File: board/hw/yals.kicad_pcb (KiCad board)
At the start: 2 copper layers, 102.9 x 16.5 mm, 46 parts, among them J1 SWD, J2 UART, J3 eng, J4 power, Q1 2N7002, U1 RP2040, U2 M24C02-FMN, U3 MCP1703Ax-330xxTT, U4 W25Q32JVSS, U5 DRV8220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

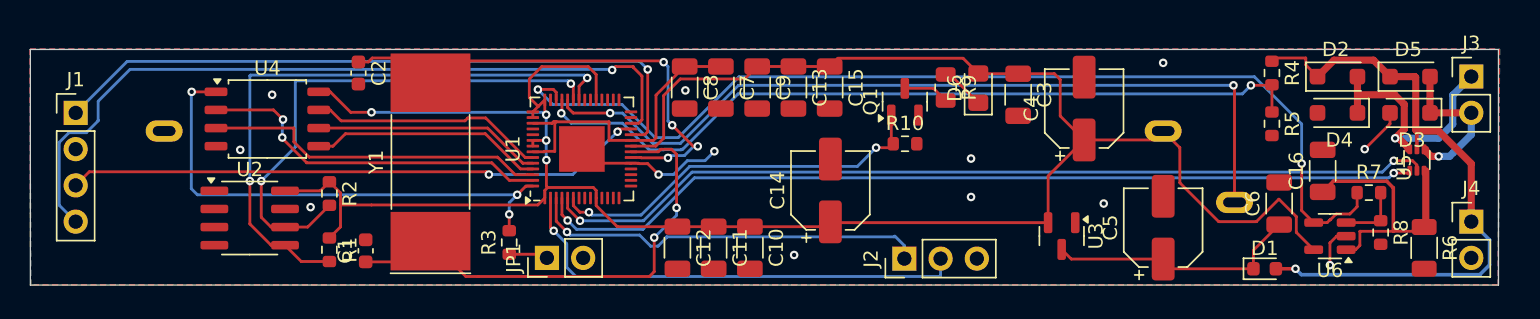
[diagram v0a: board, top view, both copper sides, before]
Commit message: increased height of the board by 1mm, to accomodate more wireing that's needed there
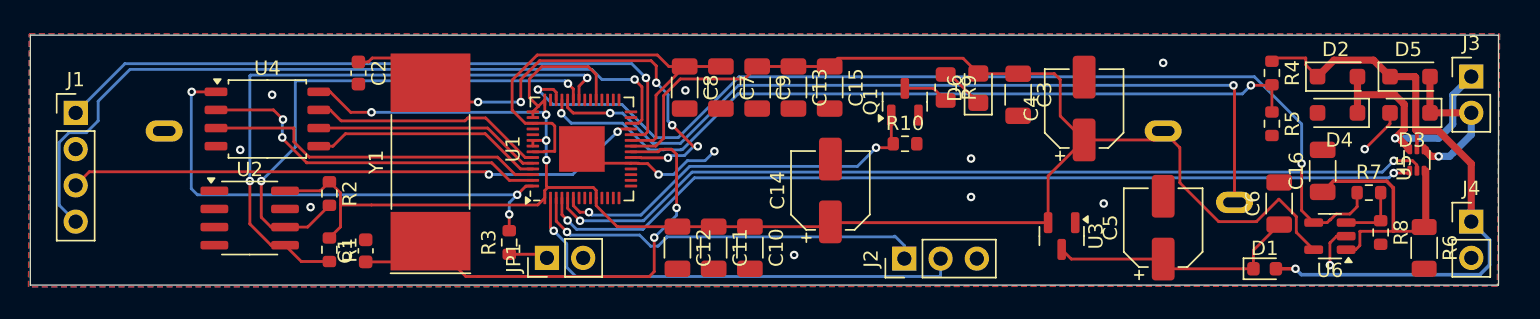
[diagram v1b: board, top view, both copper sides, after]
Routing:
- net Net-(U1-VREG_VOUT): track 22.1 -> 32.2 mm
- net Net-(U1-XIN): track 35.0 -> 38.8 mm, vias 4 -> 6
- net /microcontroller/pico_run: track 54.1 -> 53.5 mm
- net Net-(J1-Pin_1): track 47.4 -> 46.9 mm
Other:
- board size 102.9 x 16.5 mm -> 102.9 x 17.5 mm

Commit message: fixed all the DRC errors and warning on the PCB
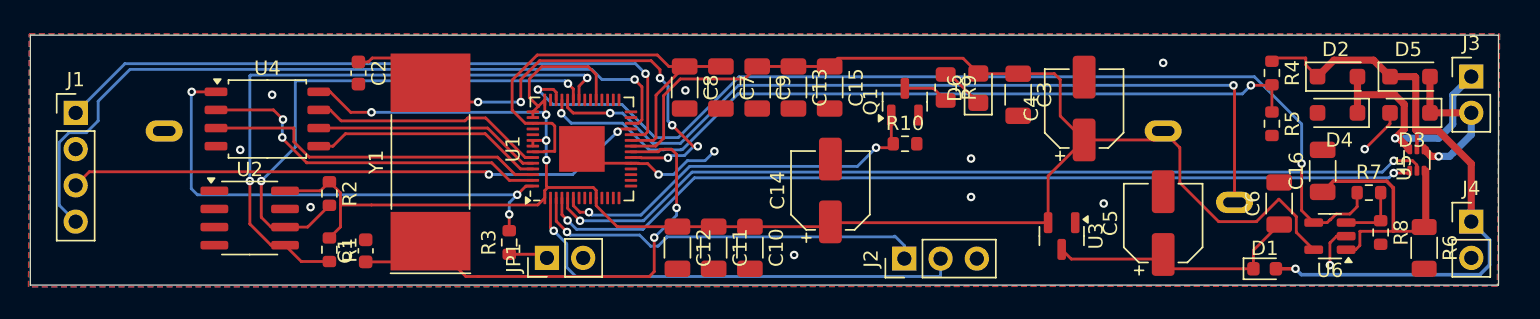
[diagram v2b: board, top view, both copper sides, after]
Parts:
- moved C5 0.32 mm to (170.2, 90.3)
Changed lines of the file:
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@@
   )
   (footprint "Capacitor_SMD:CP_Elec_5x4.5" (layer "F.Cu")
-    (at 170.18 90.592 90)
+    (at 170.18 90.2716 90)
     (descr "SMD capacitor, aluminum electrolytic, Nichicon, 5.0x4.5mm")
     (tags "capacitor electrolytic")
@@
   (segment (start 136.0836 89.7224) (end 134.5184 91.2876) (width 0.2) (layer "B.Cu") (net 36))
   (segment (start 120.375 78.905) (end 118.8425 80.4375) (width 0.2) (layer "F.Cu") (net 37))
+  (segment (start 126.485115 78.8924) (end 125.1712 80.206315) (width 0.2) (layer "F.Cu") (net 37))
+  (segment (start 134.9248 80.1116) (end 134.9248 79.520071) (width 0.2) (layer "F.Cu") (net 37))
   (segment (start 114.4812 78.981) (end 113.792 78.981) (width 0.2) (layer "F.Cu") (net 37))
   (segment (start 114.7572 78.705) (end 114.4812 78.981) (width 0.2) (layer "F.Cu") (net 37))
   (segment (start 132.8887 85.6772) (end 133.5816 85.6772) (width 0.2) (layer "F.Cu") (net 37))
-  (segment (start 126.485115 78.8924) (end 125.1712 80.206315) (width 0.2) (layer "F.Cu") (net 37))
-  (segment (start 134.297129 78.8924) (end 126.485115 78.8924) (width 0.2) (layer "F.Cu") (net 37))
-  (segment (start 134.660327 79.255598) (end 134.297129 78.8924) (width 0.2) (layer "F.Cu") (net 37))
   (segment (start 120.193 81.788) (end 118.8425 80.4375) (width 0.2) (layer "F.Cu") (net 37))
-  (segment (start 134.660327 80.440143) (end 134.660327 79.255598) (width 0.2) (layer "F.Cu") (net 37))
   (segment (start 117.11 78.705) (end 114.7572 78.705) (width 0.2) (layer "F.Cu") (net 37))
   (segment (start 118.8425 80.4375) (end 117.11 78.705) (width 0.2) (layer "F.Cu") (net 37))
@@
   (segment (start 137.255565 84.890365) (end 135.7788 83.4136) (width 0.2) (layer "F.Cu") (net 37))
   (segment (start 135.4836 85.6996) (end 133.604 85.6996) (width 0.2) (layer "F.Cu") (net 37))
+  (segment (start 137.569965 84.890365) (end 137.255565 84.890365) (width 0.2) (layer "F.Cu") (net 37))
+  (segment (start 134.9248 79.520071) (end 134.297129 78.8924) (width 0.2) (layer "F.Cu") (net 37))
+  (segment (start 122.174 81.788) (end 120.193 81.788) (width 0.2) (layer "F.Cu") (net 37))
+  (segment (start 134.297129 78.8924) (end 126.485115 78.8924) (width 0.2) (layer "F.Cu") (net 37))
   (segment (start 125.1712 80.206315) (end 125.1712 81.788) (width 0.2) (layer "F.Cu") (net 37))
-  (segment (start 137.569965 84.890365) (end 137.255565 84.890365) (width 0.2) (layer "F.Cu") (net 37))
-  (segment (start 122.174 81.788) (end 120.193 81.788) (width 0.2) (layer "F.Cu") (net 37))
   (segment (start 133.604 85.6996) (end 133.5816 85.6772) (width 0.2) (layer "F.Cu") (net 37))
   (via (at 135.4836 85.6996) (size 0.6) (drill 0.3) (layers "F.Cu" "B.Cu") (net 37))
-  (via (at 134.660327 80.440143) (size 0.6) (drill 0.3) (layers "F.Cu" "B.Cu") (net 37))
+  (via (at 134.9248 80.1116) (size 0.6) (drill 0.3) (layers "F.Cu" "B.Cu") (net 37))
   (via (at 135.7788 83.4136) (size 0.6) (drill 0.3) (layers "F.Cu" "B.Cu") (net 37))
   (via (at 122.174 81.788) (size 0.6) (drill 0.3) (layers "F.Cu" "B.Cu") (net 37))
   (via (at 125.1712 81.788) (size 0.6) (drill 0.3) (layers "F.Cu" "B.Cu") (net 37))
   (via (at 137.569965 84.890365) (size 0.6) (drill 0.3) (layers "F.Cu" "B.Cu") (net 37))
-  (segment (start 134.660327 80.440143) (end 135.4836 81.263416) (width 0.2) (layer "B.Cu") (net 37))
-  (segment (start 135.4836 83.1184) (end 135.7788 83.4136) (width 0.2) (layer "B.Cu") (net 37))
   (segment (start 137.287121 84.890365) (end 136.636685 85.5408) (width 0.2) (layer "B.Cu") (net 37))
   (segment (start 136.636685 85.5408) (end 135.6424 85.5408) (width 0.2) (layer "B.Cu") (net 37))
   (segment (start 137.569965 84.890365) (end 137.287121 84.890365) (width 0.2) (layer "B.Cu") (net 37))
   (segment (start 125.1712 81.788) (end 122.174 81.788) (width 0.2) (layer "B.Cu") (net 37))
-  (segment (start 135.4836 81.263416) (end 135.4836 83.1184) (width 0.2) (layer "B.Cu") (net 37))
+  (segment (start 135.4836 80.6704) (end 135.4836 83.1184) (width 0.2) (layer "B.Cu") (net 37))
+  (segment (start 135.4836 83.1184) (end 135.7788 83.4136) (width 0.2) (layer "B.Cu") (net 37))
+  (segment (start 134.9248 80.1116) (end 135.4836 80.6704) (width 0.2) (layer "B.Cu") (net 37))
   (segment (start 135.6424 85.5408) (end 135.4836 85.6996) (width 0.2) (layer "B.Cu") (net 37))
   (segment (start 144.272 79.297) (end 146.812 79.297) (width 0.2) (layer "F.Cu") (net 38))
@@
   (segment (start 170.86 93.472) (end 170.18 92.792) (width 0.2) (layer "F.Cu") (net 39))
   (segment (start 170.18 92.792) (end 163.744 92.792) (width 0.2) (layer "F.Cu") (net 39))
+  (segment (start 133.9088 79.8068) (end 134.0612 79.9592) (width 0.2) (layer "F.Cu") (net 40))
+  (segment (start 134.0612 83.8708) (end 133.8548 84.0772) (width 0.2) (layer "F.Cu") (net 40))
   (segment (start 133.8548 84.0772) (end 132.8887 84.0772) (width 0.2) (layer "F.Cu") (net 40))
-  (segment (start 134.0612 80.220429) (end 134.0612 83.8708) (width 0.2) (layer "F.Cu") (net 40))
-  (segment (start 133.938412 80.097641) (end 134.0612 80.220429) (width 0.2) (layer "F.Cu") (net 40))
-  (segment (start 134.0612 83.8708) (end 133.8548 84.0772) (width 0.2) (layer "F.Cu") (net 40))
-  (via (at 133.938412 80.097641) (size 0.6) (drill 0.3) (layers "F.Cu" "B.Cu") (net 40))
-  (segment (start 133.938412 80.097641) (end 132.942771 79.102) (width 0.2) (layer "B.Cu") (net 40))
+  (segment (start 134.0612 79.9592) (end 134.0612 83.8708) (width 0.2) (layer "F.Cu") (net 40))
+  (via (at 133.9088 79.8068) (size 0.6) (drill 0.3) (layers "F.Cu" "B.Cu") (net 40))
   (segment (start 97.428 79.102) (end 93.98 82.55) (width 0.2) (layer "B.Cu") (net 40))
-  (segment (start 132.942771 79.102) (end 97.428 79.102) (width 0.2) (layer "B.Cu") (net 40))
+  (segment (start 133.204 79.102) (end 97.428 79.102) (width 0.2) (layer "B.Cu") (net 40))
+  (segment (start 133.9088 79.8068) (end 133.204 79.102) (width 0.2) (layer "B.Cu") (net 40))
   (segment (start 93.98 87.63) (end 94.934 86.676) (width 0.2) (layer "F.Cu") (net 41))
   (segment (start 131.9924 83.6772) (end 132.8887 83.6772) (width 0.2) (layer "F.Cu") (net 41))

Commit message: moved power connection a bit higher, to be away from the board
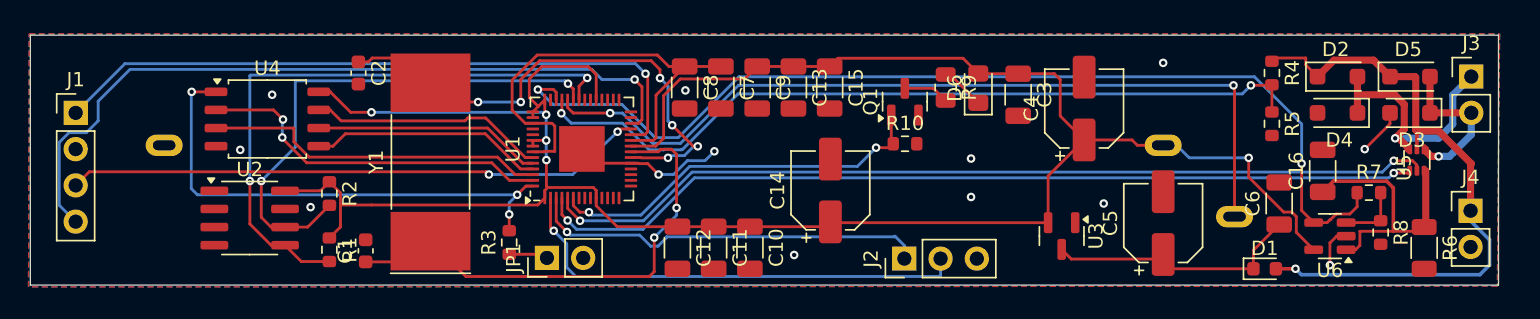
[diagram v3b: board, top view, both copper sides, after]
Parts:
- moved RV1 1.00 mm to (135.2, 87.3)
- moved J4 0.77 mm to (191.7, 89.4)
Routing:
- net +3.3V: track 165.2 -> 162.8 mm, vias 4 -> 5
- net /engine ctrl/eng_pos_feedback: track 58.1 -> 59.1 mm
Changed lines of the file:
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@@
   )
   (footprint "Connector_PinHeader_2.54mm:PinHeader_1x02_P2.54mm_Vertical" (layer "F.Cu")
-    (at 191.77 90.17)
+    (at 191.7192 89.403)
     (descr "Through hole straight pin header, 1x02, 2.54mm pitch, single row")
     (tags "Through hole pin header THT 1x02 2.54mm single row")
@@
   )
   (footprint "st_passives_potentiometers:CDE23N-60-B50K" (layer "B.Cu")
-    (at 135.18 86.32 180)
+    (at 135.18 87.32 180)
     (property "Sheetfile" "engine_ctrl.kicad_sch")
     (property "Sheetname" "engine ctrl")
@@
   (segment (start 187.8236 80.01) (end 187.8744 80.0608) (width 0.5) (layer "F.Cu") (net 35))
   (segment (start 180.175 78.705) (end 178.026 78.705) (width 0.2) (layer "F.Cu") (net 35))
+  (segment (start 191.7192 86.1568) (end 191.7192 89.403) (width 0.5) (layer "F.Cu") (net 35))
   (segment (start 186.0744 80.01) (end 187.8236 80.01) (width 0.5) (layer "F.Cu") (net 35))
-  (segment (start 191.77 90.17) (end 191.77 86.106) (width 0.5) (layer "F.Cu") (net 35))
   (segment (start 191.77 86.106) (end 189.484 83.82) (width 0.5) (layer "F.Cu") (net 35))
   (segment (start 184.9194 78.855) (end 182.1494 78.855) (width 0.5) (layer "F.Cu") (net 35))
@@
   (segment (start 182.1494 78.855) (end 180.9944 80.01) (width 0.5) (layer "F.Cu") (net 35))
   (segment (start 187.96 85.102) (end 187.96 83.82) (width 0.25) (layer "F.Cu") (net 35))
+  (segment (start 191.77 86.106) (end 191.7192 86.1568) (width 0.5) (layer "F.Cu") (net 35))
   (segment (start 178.026 78.705) (end 177.8 78.931) (width 0.2) (layer "F.Cu") (net 35))
   (segment (start 187.8744 83.7344) (end 187.96 83.82) (width 0.5) (layer "F.Cu") (net 35))
@@
   (segment (start 192.373 93.885) (end 193.05 93.208) (width 0.25) (layer "B.Cu") (net 35))
   (segment (start 193.05 93.208) (end 193.05 91.45) (width 0.25) (layer "B.Cu") (net 35))
+  (segment (start 191.77 89.4538) (end 191.7192 89.403) (width 0.25) (layer "B.Cu") (net 35))
+  (segment (start 191.77 90.17) (end 191.77 89.4538) (width 0.25) (layer "B.Cu") (net 35))
   (segment (start 136.0836 89.2048) (end 136.0836 85.451071) (width 0.2) (layer "F.Cu") (net 36))
   (segment (start 117.39 92.99) (end 118.8425 91.5375) (width 0.2) (layer "F.Cu") (net 36))
@@
   (segment (start 146.9182 90.241) (end 146.8628 90.1856) (width 0.2) (layer "F.Cu") (net 38))
   (segment (start 113.248799 82.5088) (end 114.7064 82.5088) (width 0.2) (layer "F.Cu") (net 38))
-  (segment (start 176.713144 90.17) (end 174.070812 90.17) (width 0.2) (layer "F.Cu") (net 38))
   (segment (start 136.144 90.522) (end 131.92464 90.522) (width 0.2) (layer "F.Cu") (net 38))
   (segment (start 126.8512 81.6397) (end 126.39425 82.09665) (width 0.2) (layer "F.Cu") (net 38))
@@
   (segment (start 162.9664 82.7688) (end 164.6428 84.4452) (width 0.2) (layer "F.Cu") (net 38))
   (segment (start 130.4512 87.98084) (end 130.4512 88.5147) (width 0.2) (layer "F.Cu") (net 38))
+  (segment (start 167.9956 84.4452) (end 168.3704 84.82) (width 0.2) (layer "F.Cu") (net 38))
   (segment (start 114.7064 89.0016) (end 126.3643 89.0016) (width 0.2) (layer "F.Cu") (net 38))
   (segment (start 126.8512 82.5792) (end 126.8512 81.6397) (width 0.2) (layer "F.Cu") (net 38))
@@
   (segment (start 112.5858 89.0016) (end 112.535 88.9508) (width 0.2) (layer "F.Cu") (net 38))
   (segment (start 126.0137 82.4772) (end 126.0137 82.8772) (width 0.2) (layer "F.Cu") (net 38))
-  (segment (start 171.3484 87.447588) (end 171.3484 84.9884) (width 0.2) (layer "F.Cu") (net 38))
+  (segment (start 180.7265 92.136) (end 179.508 90.9175) (width 0.2) (layer "F.Cu") (net 38))
   (segment (start 160.02 79.805) (end 162.5582 79.805) (width 0.2) (layer "F.Cu") (net 38))
   (segment (start 162.5582 79.805) (end 162.9664 80.2132) (width 0.2) (layer "F.Cu") (net 38))
-  (segment (start 171.3484 84.9884) (end 170.18 83.82) (width 0.2) (layer "F.Cu") (net 38))
+  (segment (start 176.1744 87.051144) (end 176.1744 85.6996) (width 0.2) (layer "F.Cu") (net 38))
   (segment (start 125.766885 81.469285) (end 126.39425 82.09665) (width 0.2) (layer "F.Cu") (net 38))
   (segment (start 160.02 79.805) (end 157.2422 79.805) (width 0.2) (layer "F.Cu") (net 38))
   (segment (start 125.766885 80.176315) (end 125.766885 81.469285) (width 0.2) (layer "F.Cu") (net 38))
   (segment (start 138.684 90.522) (end 141.224 90.522) (width 0.2) (layer "F.Cu") (net 38))
-  (segment (start 179.508 90.9175) (end 179.508 89.815256) (width 0.2) (layer "F.Cu") (net 38))
   (segment (start 112.535 88.151) (end 111.76 87.376) (width 0.2) (layer "F.Cu") (net 38))
+  (segment (start 168.3704 84.82) (end 170.18 84.82) (width 0.2) (layer "F.Cu") (net 38))
+  (segment (start 179.508 89.815256) (end 179.192744 89.5) (width 0.2) (layer "F.Cu") (net 38))
   (segment (start 126.9492 82.6772) (end 126.8512 82.5792) (width 0.2) (layer "F.Cu") (net 38))
   (segment (start 126.6382 79.305) (end 125.766885 80.176315) (width 0.2) (layer "F.Cu") (net 38))
@@
   (segment (start 126.0137 84.4772) (end 126.0137 84.8772) (width 0.2) (layer "F.Cu") (net 38))
   (segment (start 111.125 88.011) (end 111.76 87.376) (width 0.2) (layer "F.Cu") (net 38))
-  (segment (start 179.508 89.815256) (end 178.287944 88.5952) (width 0.2) (layer "F.Cu") (net 38))
+  (segment (start 179.192744 89.5) (end 178.623256 89.5) (width 0.2) (layer "F.Cu") (net 38))
   (segment (start 157.2422 79.805) (end 157.226 79.7888) (width 0.2) (layer "F.Cu") (net 38))
   (segment (start 162.118 90.241) (end 162.118 86.97) (width 0.2) (layer "F.Cu") (net 38))
-  (segment (start 180.7265 92.136) (end 179.508 90.9175) (width 0.2) (layer "F.Cu") (net 38))
   (segment (start 130.24756 87.7772) (end 130.4512 87.98084) (width 0.2) (layer "F.Cu") (net 38))
   (segment (start 126.948 84.4772) (end 126.9512 84.4804) (width 0.2) (layer "F.Cu") (net 38))
   (segment (start 162.118 90.241) (end 146.9182 90.241) (width 0.2) (layer "F.Cu") (net 38))
-  (segment (start 174.070812 90.17) (end 171.3484 87.447588) (width 0.2) (layer "F.Cu") (net 38))
   (segment (start 129.8956 79.305) (end 126.6382 79.305) (width 0.2) (layer "F.Cu") (net 38))
+  (segment (start 164.6428 84.4452) (end 167.9956 84.4452) (width 0.2) (layer "F.Cu") (net 38))
   (segment (start 130.4512 89.04856) (end 130.4512 88.5147) (width 0.2) (layer "F.Cu") (net 38))
   (segment (start 156.1592 78.722) (end 157.226 79.7888) (width 0.2) (layer "F.Cu") (net 38))
   (segment (start 127.05484 87.7772) (end 130.24756 87.7772) (width 0.2) (layer "F.Cu") (net 38))
-  (segment (start 164.6428 84.4452) (end 169.5548 84.4452) (width 0.2) (layer "F.Cu") (net 38))
-  (segment (start 178.287944 88.5952) (end 176.713144 90.17) (width 0.2) (layer "F.Cu") (net 38))
   (segment (start 162.118 86.97) (end 164.6428 84.4452) (width 0.2) (layer "F.Cu") (net 38))
   (segment (start 126.39425 82.09665) (end 126.0137 82.4772) (width 0.2) (layer "F.Cu") (net 38))
   (segment (start 126.964191 85.855752) (end 126.964191 87.686551) (width 0.2) (layer "F.Cu") (net 38))
-  (segment (start 169.5548 84.4452) (end 170.18 83.82) (width 0.2) (layer "F.Cu") (net 38))
   (segment (start 135.1788 84.328) (end 134.6296 84.8772) (width 0.2) (layer "F.Cu") (net 38))
   (segment (start 140.857 80.172) (end 136.342686 80.172) (width 0.2) (layer "F.Cu") (net 38))
@@
   (segment (start 126.8512 87.98084) (end 127.05484 87.7772) (width 0.2) (layer "F.Cu") (net 38))
   (segment (start 162.9664 80.2132) (end 162.9664 82.7688) (width 0.2) (layer "F.Cu") (net 38))
+  (segment (start 179.508 90.9175) (end 179.508 89.815256) (width 0.2) (layer "F.Cu") (net 38))
+  (segment (start 178.623256 89.5) (end 176.1744 87.051144) (width 0.2) (layer "F.Cu") (net 38))
+  (via (at 176.1744 85.6996) (size 0.6) (drill 0.3) (layers "F.Cu" "B.Cu") (net 38))
   (via (at 126.9492 82.6772) (size 0.6) (drill 0.3) (layers "F.Cu" "B.Cu") (net 38))
   (via (at 126.9512 84.4804) (size 0.6) (drill 0.3) (layers "F.Cu" "B.Cu") (net 38))
   (via (at 126.964191 85.855752) (size 0.6) (drill 0.3) (layers "F.Cu" "B.Cu") (net 38))
   (via (at 114.7064 82.5088) (size 0.6) (drill 0.3) (layers "F.Cu" "B.Cu") (net 38))
+  (segment (start 172.0088 85.6996) (end 171.1292 84.82) (width 0.2) (layer "B.Cu") (net 38))
   (segment (start 126.7808 82.5088) (end 126.9492 82.6772) (width 0.2) (layer "B.Cu") (net 38))
   (segment (start 126.9512 85.842761) (end 126.964191 85.855752) (width 0.2) (layer "B.Cu") (net 38))
+  (segment (start 176.1744 85.6996) (end 172.0088 85.6996) (width 0.2) (layer "B.Cu") (net 38))
   (segment (start 126.9512 84.4804) (end 126.9512 85.842761) (width 0.2) (layer "B.Cu") (net 38))
   (segment (start 126.9492 84.4784) (end 126.9512 84.4804) (width 0.2) (layer "B.Cu") (net 38))
+  (segment (start 171.1292 84.82) (end 170.18 84.82) (width 0.2) (layer "B.Cu") (net 38))
   (segment (start 126.9492 82.6772) (end 126.9492 84.4784) (width 0.2) (layer "B.Cu") (net 38))
   (segment (start 114.7064 82.5088) (end 126.7808 82.5088) (width 0.2) (layer "B.Cu") (net 38))
@@
   (segment (start 128.4512 81.6397) (end 128.4512 82.17356) (width 0.2) (layer "F.Cu") (net 46))
   (segment (start 128.4512 82.17356) (end 128.839995 82.562355) (width 0.2) (layer "F.Cu") (net 46))
-  (segment (start 175.1076 80.6196) (end 175.18 80.692) (width 0.2) (layer "F.Cu") (net 46))
+  (segment (start 175.18 80.692) (end 175.1076 80.6196) (width 0.2) (layer "F.Cu") (net 46))
+  (segment (start 175.18 89.82) (end 175.18 80.692) (width 0.2) (layer "F.Cu") (net 46))
   (segment (start 128.839995 82.562355) (end 131.429348 82.562355) (width 0.2) (layer "F.Cu") (net 46))
-  (segment (start 175.18 80.692) (end 175.18 88.82) (width 0.2) (layer "F.Cu") (net 46))
   (via (at 131.429348 82.562355) (size 0.6) (drill 0.3) (layers "F.Cu" "B.Cu") (net 46))
   (via (at 175.1076 80.6196) (size 0.6) (drill 0.3) (layers "F.Cu" "B.Cu") (net 46))

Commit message: added proper soldermask marking of all I/O pins + moved element designators to rightful places
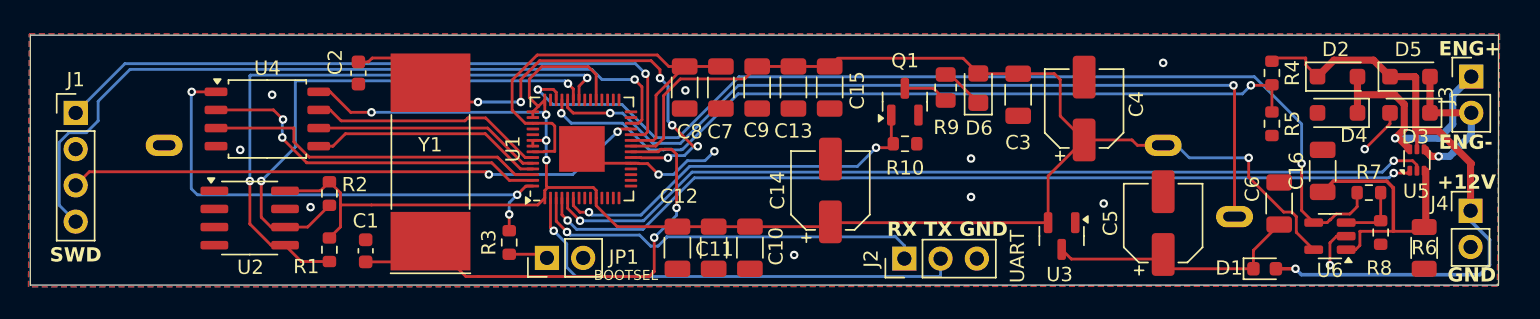
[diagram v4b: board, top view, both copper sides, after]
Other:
- board text added: "+12V"
- board text added: "ENG+"
- board text added: "ENG-"
- board text added: "GND"
- board text added: "RX TX GND"
